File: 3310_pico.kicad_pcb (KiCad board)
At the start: 4 copper layers, 41.7 x 110 mm, 47 parts, among them J4 PCDTest, J5 KeypadTest, J6 BuzzerTest, Q1 2N3904, Q2 2N3904, Q3 2N3904

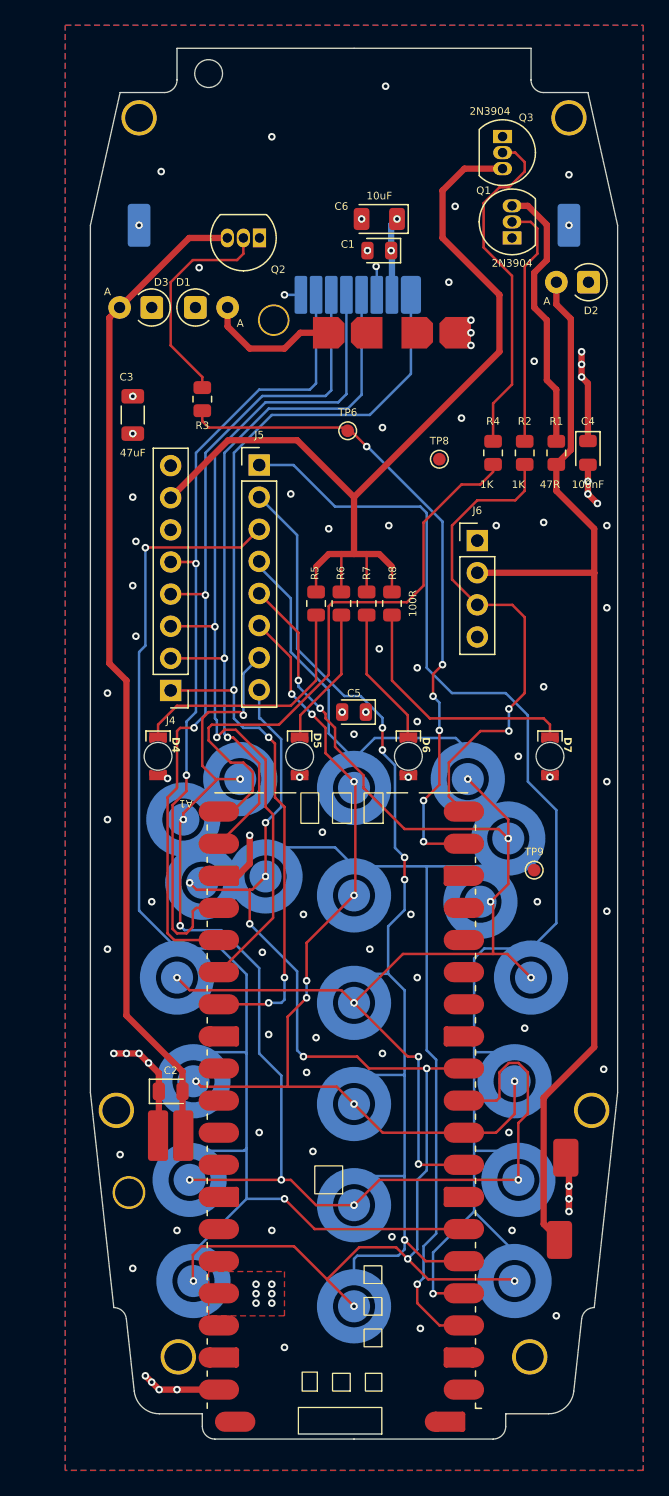
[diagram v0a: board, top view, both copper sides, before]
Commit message: Revision 1 with battery charging, rgb backlight, etc
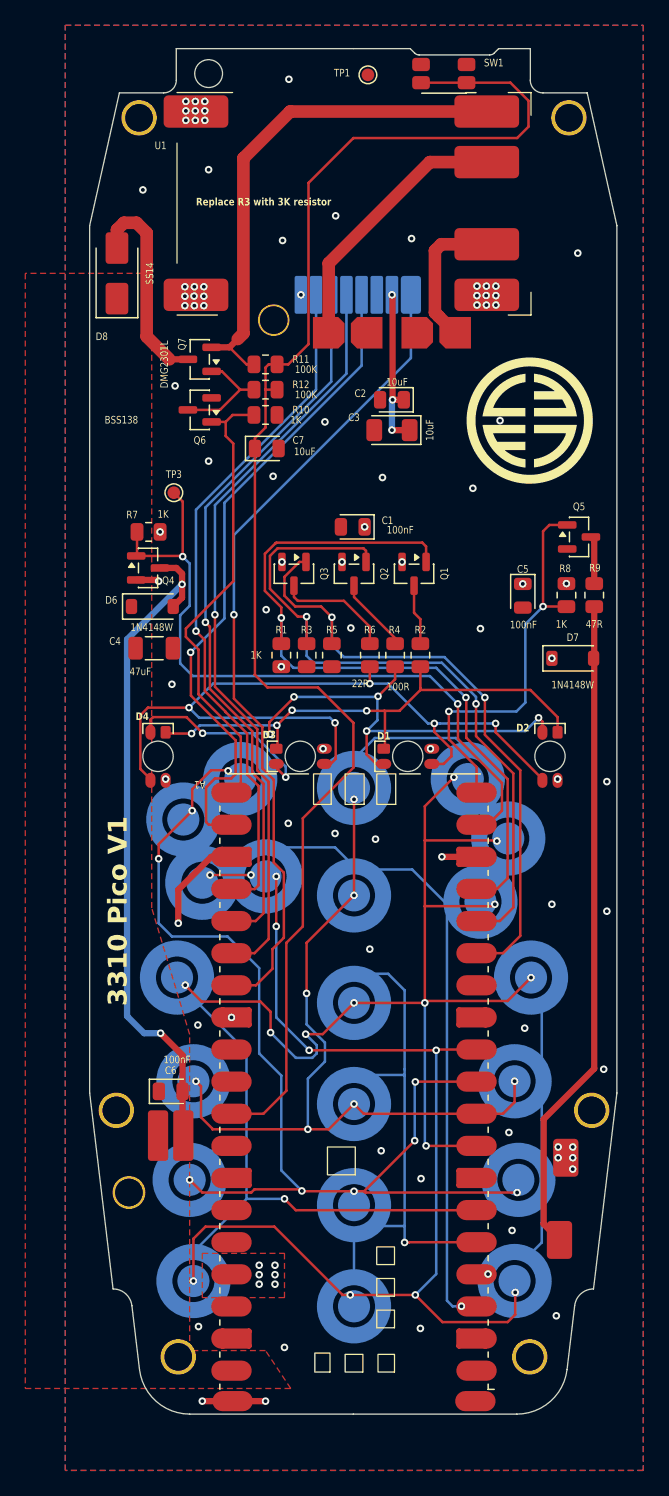
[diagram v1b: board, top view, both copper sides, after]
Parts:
- removed D5: LED, 3310Footprints:VoidLED
- removed the J4 at (145.5, 95.8)
- removed J5: KeypadTest, Connector_PinHeader_2.54mm:PinHeader_1x08_P2.54mm_Vertical
- removed the J6 at (169.8, 83.9)
- removed the R8 at (163.0, 88.9)
- removed REF** (x2): TestPoint_Keystone_5015_Micro_Mini, TestPoint:TestPoint_Keystone_5015_Micro_Mini
- removed TP9: TestPoint, TestPoint:TestPoint_Pad_D1.0mm
- added C7: 10uF, Diode_SMD:D_0805_2012Metric, F.Cu at (153.1, 76.7)
- added D8: SS14, Diode_SMD:D_SMA, F.Cu at (141.2, 62.8)
- added G***: LOGO, LOGO, F.Cu at (173.9, 74.5)
- added Q4: BSS138, Package_TO_SOT_SMD:SOT-23, F.Cu at (143.7, 86.1)
- added Q5: BSS138, Package_TO_SOT_SMD:SOT-23, F.Cu at (177.8, 83.7)
- added Q6: BSS138, Package_TO_SOT_SMD:SOT-23, F.Cu at (147.8, 73.6)
- added Q7: DMG2301L, Package_TO_SOT_SMD:SOT-23, F.Cu at (147.8, 69.6)
- added R10: 1K, Resistor_SMD:R_0805_2012Metric, F.Cu at (153.0, 74.0)
- added R11: 100K, Resistor_SMD:R_0805_2012Metric, F.Cu at (153.0, 70.0)
- added R12: 100K, Resistor_SMD:R_0805_2012Metric, F.Cu at (153.0, 72.0)
- added R3: 1K, Resistor_SMD:R_0805_2012Metric, F.Cu at (156.2, 93.0)
- added R5: 1K, Resistor_SMD:R_0805_2012Metric, F.Cu at (158.2, 93.0)
- added SW1: EVQP7A, Button_Switch_SMD:SW_SPST_EVQP7A, F.Cu at (167.1, 47.0)
- added U1: ~, 3310Footprints:TP4056_charger, F.Cu at (146.0, 48.5)
- D1, D2, D3: value D -> ~; footprint Diode_THT:D_A-405_P2.54mm_Vertical_AnodeUp -> 3310Footprints:VoidRGB
- D4: value LED -> ~; footprint 3310Footprints:VoidLED -> 3310Footprints:VoidRGB
- D6, D7: value LED -> 1N4148W; footprint 3310Footprints:VoidLED -> Diode_SMD:D_SOD-123
- Q1, Q2, Q3: value 2N3904 -> BSS138; footprint Package_TO_SOT_THT:TO-92_Inline -> Package_TO_SOT_SMD:SOT-23
- R2: renamed from R5; value 100R -> 82R
- R6: renamed from R7; value 100R -> 22R
- moved D1 39.3 mm to (164.2, 101.0), turned to 180 degrees
- moved Q3 38.3 mm to (155.2, 86.6)
- moved D2 37.6 mm to (175.5, 101.0), turned to 90 degrees
- moved D3 37.4 mm to (155.8, 101.0)
- moved TP1 30.9 mm to (161.1, 47.1)
- moved Q1 27.7 mm to (164.8, 86.6), turned to -90 degrees
- moved Q2 27.6 mm to (160.0, 86.6), turned to -90 degrees
- moved D6 23.5 mm to (144.1, 89.2), turned to 0 degrees
- moved R1 23.2 mm to (154.2, 93.0), turned to -90 degrees
- moved C4 18.5 mm to (144.2, 92.5), turned to 0 degrees
- moved C3 16.7 mm to (163.0, 75.2)
- moved C1 14.7 mm to (159.9, 82.8)
- moved TP3 14.6 mm to (145.8, 80.2)
- moved C5 12.4 mm to (173.3, 88.3)
- moved C2 11.8 mm to (163.0, 72.8)
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- renumbered C5 to C1, C1 to C2, C6 to C3, C3 to C4, C4 to C5, C2 to C6, J3 to J4, J2 to J6, R4 to R1, R6 to R4, R3 to R7, R2 to R8, R1 to R9, TP8 to TP1, TP6 to TP3
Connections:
- ? pad 1: GND -> (no net)
- A1 pad 15: unconnected-(A1-GPIO11-Pad15) -> /BacklightB
- A1 pad 16: unconnected-(A1-GPIO12-Pad16) -> /BacklightG
- A1 pad 17: unconnected-(A1-GPIO13-Pad17) -> /BacklightR
- A1 pad 21: /Backlight -> /PowerLatch
- A1 pad 31: unconnected-(A1-GPIO26_ADC0-Pad31) -> /VBattMeas
- C6 pad 2: Net-(D3-A) -> Net-(D6-A)
- D1 pad 1: Vdrive -> Net-(D1-RK)
- D1 pad 2: +BATT -> +3.3V
- D2 pad 1: +3.3V -> Net-(D1-RK)
- D2 pad 2: /BuzzerOut -> +3.3V
- D3 pad 1: Vdrive -> Net-(D1-RK)
- D3 pad 2: Net-(D3-A) -> +3.3V
- D4 pad 1: Net-(D4-K) -> Net-(D1-RK)
- D6 pad 1: Net-(D6-K) -> Vdrive
- D6 pad 2: +3.3V -> Net-(D6-A)
- D7 pad 1: Net-(D7-K) -> +3.3V
- D7 pad 2: +3.3V -> /BuzzerOut
- J6 pad 4: GND -> -BATT
- M1 pad 2: Net-(D3-A) -> Net-(D6-A)
- Q1 pad 1: GND -> /BacklightR
- Q1 pad 2: Net-(Q1-B) -> GND
- Q1 pad 3: Net-(Q1-C) -> Net-(Q1-D)
- Q2 pad 1: GND -> /BacklightG
- Q2 pad 2: Net-(Q2-B) -> GND
- Q2 pad 3: Net-(D3-A) -> Net-(Q2-D)
- Q3 pad 1: GND -> /BacklightB
- Q3 pad 2: Net-(Q3-B) -> GND
- Q3 pad 3: /BacklightOut -> Net-(Q3-D)
- R1 pad 1: /Backlight -> /BacklightR
- R1 pad 2: Net-(Q3-B) -> GND
- R2 pad 1: Net-(D4-K) -> Net-(D1-RK)
- R2 pad 2: /BacklightOut -> Net-(Q1-D)
- R4 pad 1: Net-(D5-K) -> Net-(D1-GK)
- R4 pad 2: /BacklightOut -> Net-(Q2-D)
- R6 pad 1: Net-(D6-K) -> Net-(D1-BK)
- R6 pad 2: /BacklightOut -> Net-(Q3-D)
- R7 pad 1: /Vibe -> GND
- R7 pad 2: Net-(Q2-B) -> /Vibe
- R8 pad 2: Net-(Q1-B) -> GND
- R9 pad 2: Net-(Q1-C) -> Net-(Q5-D)
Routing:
- net /VBattMeas: track 0.00 -> 118.6 mm
- net /Col1: track 103.2 -> 22.8 mm
- net Net-(D3-A): track 79.1 -> 0.00 mm
- net /BacklightOut: track 75.9 -> 0.00 mm
- net Net-(D1-BK): track 0.00 -> 64.2 mm, vias 0 -> 5
- net /BacklightR: track 0.00 -> 59.5 mm, vias 0 -> 2
- net /BacklightG: track 0.00 -> 56.4 mm, vias 0 -> 2
- net Net-(D6-A): track 0.00 -> 52.8 mm, vias 0 -> 2
- net Net-(D1-GK): track 0.00 -> 52.7 mm, vias 0 -> 7
- net /BacklightB: track 0.00 -> 50.3 mm, vias 0 -> 2
- net /Col3: track 99.8 -> 50.8 mm, vias 2 -> 1
- net /Backlight: track 48.0 -> 0.00 mm
- net /Col2: track 88.0 -> 41.7 mm, vias 5 -> 1
- net Net-(D1-RK): track 0.00 -> 41.3 mm, vias 0 -> 4
- net Net-(Q7-S): track 0.00 -> 40.1 mm
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- added copper zone on In2.Cu, net VBUS
- added copper zone on F.Cu, net Vdrive
- removed copper zone on In2.Cu, net Vdrive
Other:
- board size 41.7 x 110 mm -> 41.7 x 108 mm
- board text added: "3310 Pico V1"
